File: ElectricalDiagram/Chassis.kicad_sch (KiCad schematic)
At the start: 0 parts

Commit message: Prepped Electrical Diagram for meeting
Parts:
- added J10, J11, J12, J13, J14, J16, J17, J18, J22, J23, J25, J26, J29, J3, J30, J4, J5, J6, J7, J8, J9: Conn_01x02, symbol Connector_Generic:Conn_01x02
- added J15: Conn_01x08_Pin, symbol Connector:Conn_01x08_Pin
- added J19, J20, J21, J24, J27, J28: Conn_01x04_Pin, symbol Connector:Conn_01x04_Pin
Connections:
- new net +19V: J15.7 (Pin_7)
- new net +24V_Chassis: J10.2 (Pin_2), J14.2 (Pin_2), J7.2 (Pin_2), J8.2 (Pin_2), J9.2 (Pin_2)
- new net +24V_Gimbal: J15.6 (Pin_6), J16.2 (Pin_2), J25.2 (Pin_2), J26.2 (Pin_2)
- new net +24V_Shooter: J13.2 (Pin_2), J15.5 (Pin_5)
- new net +3.3V: J21.4 (Pin_4), J28.4 (Pin_4)
- new net +3V3: J20.4 (Pin_4), J27.4 (Pin_4)
- new net +5V: J15.8 (Pin_8), J18.2 (Pin_2)
- new net CAN+: J11.2 (Pin_2), J12.2 (Pin_2), J22.2 (Pin_2), J23.2 (Pin_2), J3.2 (Pin_2), J4.2 (Pin_2), J5.2 (Pin_2), J6.2 (Pin_2)
- new net CAN-: J11.1 (Pin_1), J12.1 (Pin_1), J22.1 (Pin_1), J23.1 (Pin_1), J3.1 (Pin_1), J4.1 (Pin_1), J5.1 (Pin_1), J6.1 (Pin_1)
- new net CAN2+: J29.2 (Pin_2), J30.2 (Pin_2)
- new net CAN2-: J29.1 (Pin_1), J30.1 (Pin_1)
- new net GND: J10.1 (Pin_1), J13.1 (Pin_1), J14.1 (Pin_1), J15.1 (Pin_1), J15.2 (Pin_2), J15.3 (Pin_3), J15.4 (Pin_4), J16.1 (Pin_1), J17.1 (Pin_1), J18.1 (Pin_1), J20.1 (Pin_1), J21.1 (Pin_1), J25.1 (Pin_1), J26.1 (Pin_1), J27.1 (Pin_1), J28.1 (Pin_1), J7.1 (Pin_1), J8.1 (Pin_1), J9.1 (Pin_1)
- new net GND1: J19.1 (Pin_1), J24.1 (Pin_1)
- new net Mini_PC: J17.2 (Pin_2)
- new net REF_CAN+: J19.3 (Pin_3), J24.3 (Pin_3)
- new net REF_CAN-: J19.2 (Pin_2), J24.2 (Pin_2)
- new net REF_PWR: J19.4 (Pin_4), J24.4 (Pin_4)
- new net SWCLK: J21.2 (Pin_2), J28.2 (Pin_2)
- new net SWDIO: J21.3 (Pin_3), J28.3 (Pin_3)
- new net UART_RX: J20.3 (Pin_3), J27.3 (Pin_3)
- new net UART_TX: J20.2 (Pin_2), J27.2 (Pin_2)
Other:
- note added: "CAN I/O"
- note added: "CAN Passthrough"
- note added: "GIM 1"
- note added: "GIM 2"
- note added: "Power Inputs (PMM & Dev Board)"
- note added: "Power Outputs"
- note added: "REF System"
- note added: "Serial Debug"
- note added: "UART!"
- note added: "to BL ESC"
- note added: "to BR ESC"
- note added: "to FL ESC"
- note added: "to FR ESC"

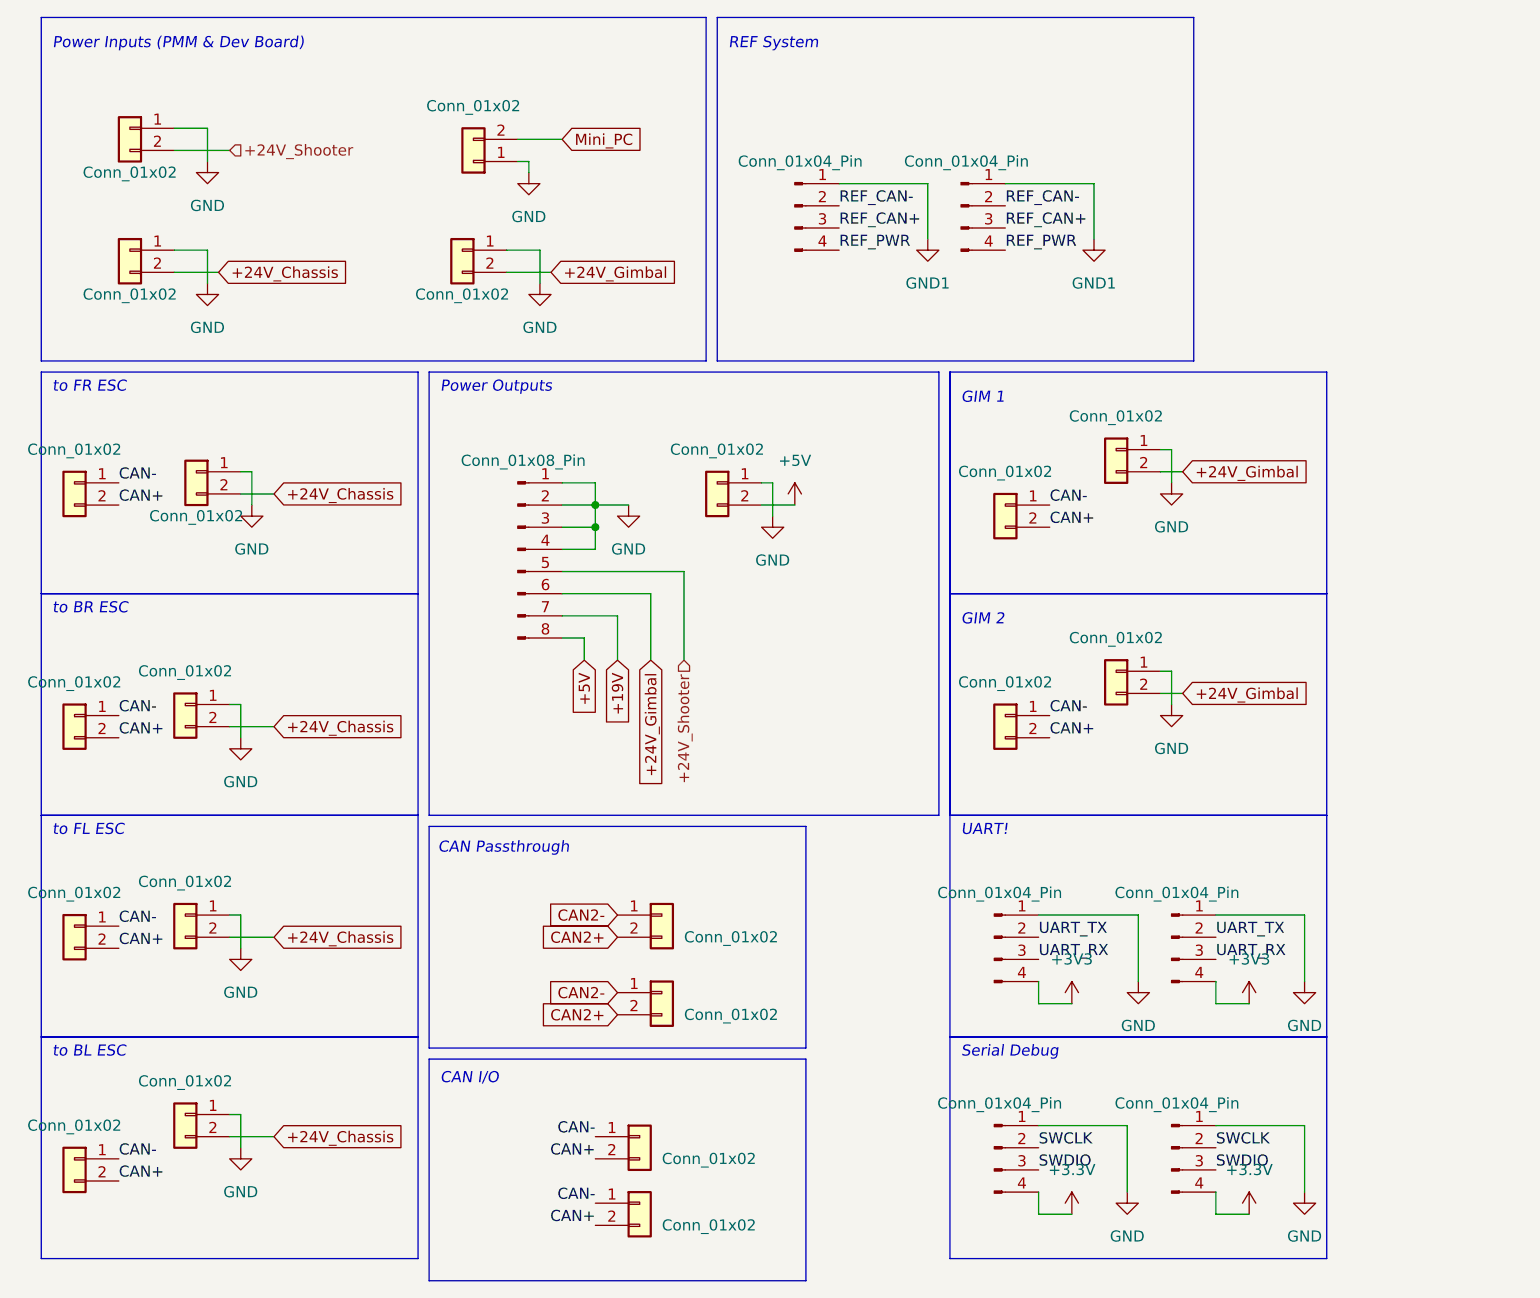
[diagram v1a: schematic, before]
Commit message: Added hierarchial labels to chassis board, please look over
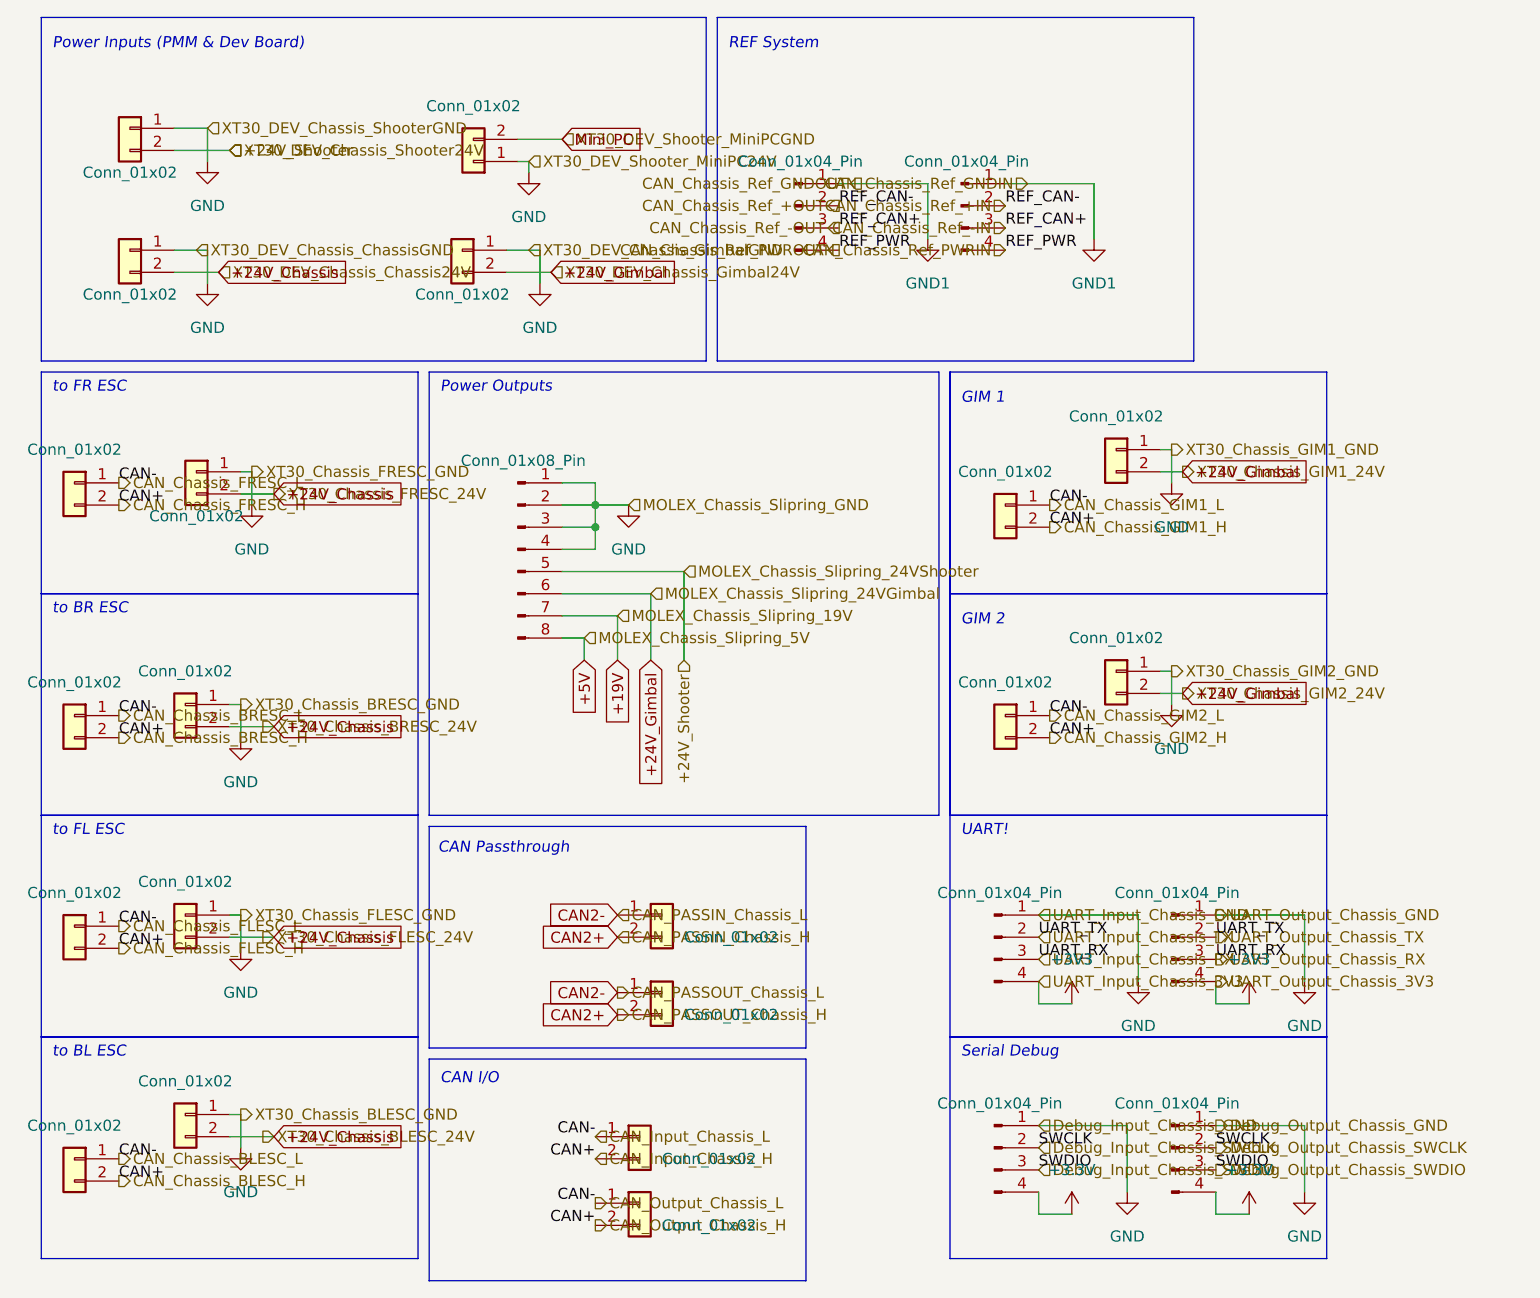
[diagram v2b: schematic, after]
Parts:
- removed J18: Conn_01x02, symbol Connector_Generic:Conn_01x02
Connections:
- net CAN+ renamed CAN_Chassis_BLESC_H
- net CAN- renamed CAN_Chassis_BLESC_L
- net REF_CAN+ renamed CAN_Chassis_Ref_-IN
- net REF_CAN- renamed CAN_Chassis_Ref_+IN
- net REF_PWR renamed CAN_Chassis_Ref_PWRIN
- net SWCLK renamed Debug_Input_Chassis_SWCLK
- net SWDIO renamed Debug_Input_Chassis_SWDIO
- net UART_RX renamed UART_Input_Chassis_RX
- net UART_TX renamed UART_Input_Chassis_TX
